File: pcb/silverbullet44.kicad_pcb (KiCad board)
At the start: 2 copper layers, 155.6 x 105.4 mm, 88 parts, among them J1 Conn_01x01, J2 Conn_01x01, J3 Conn_01x01, J4 Conn_01x01, J5 Conn_01x01, SW1 SW_PUSH, SW10 SW_PUSH, SW11 SW_PUSH, SW12 SW_PUSH, SW13 SW_PUSH, SW14 SW_PUSH, SW15 SW_PUSH, SW16 SW_PUSH, SW17 SW_PUSH, SW18 SW_PUSH, SW19 SW_PUSH, SW2 SW_PUSH, SW20 SW_PUSH, SW21 SW_PUSH, SW22 SW_PUSH, SW23 SW_PUSH, SW3 SW_PUSH, SW4 SW_PUSH, SW5 SW_PUSH, SW6 SW_PUSH, SW7 SW_PUSH, SW8 SW_PUSH, SW9 SW_PUSH, U1 ProMicro

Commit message: via
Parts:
- D1, D10, D11, D12, D13, D14, D15, D16, D17, D18, D19, D2, D20, D21, D22, D23, D3, D4, D5, D6, D7, D8, D9: footprint kbd:D3_SMD -> Keyboard:D3_SMD_revese
- J3, J4, J5: footprint keebio_parts:SolidCopper -> MountingHole:MountingHole_2.2mm_M2_Pad_Via
- L1, L10, L11, L12, L13, L14, L15, L16, L17, L18, L19, L2, L20, L21, L22, L3, L4, L5, L6, L7, L8, L9: value SK6812MINI -> YS-SK6812MINI; footprint kbd:SK6812MINI_rev -> Keyboard:YS-SK6812MINI-E-reverse
- SW1, SW10, SW11, SW12, SW13, SW14, SW15, SW16, SW17, SW18, SW2, SW21, SW3, SW4, SW5, SW6, SW7, SW8, SW9: footprint kbd:CherryMX_Hotswap -> Keyboard:MX_Hotswap_R_1u
- SW19, SW20: footprint kbd:CherryMX_Hotswap_1.5u -> Keyboard:MX_Hotswap_R_1.5u
- SW22: footprint kbd:CherryMX_Hotswap -> Keyboard:MX_Hotswap_R_1.25u
- moved L22 127.6 mm to (75.9, 106.6), turned to 300 degrees
- moved L20 96.3 mm to (112.4, 102.9)
- moved L21 92.6 mm to (92.5, 96.9), turned to 300 degrees
- moved L19 89.2 mm to (125.7, 94.6), turned to 90 degrees
- moved L4 61.6 mm to (163.8, 29.2)
- moved L5 58.0 mm to (182.9, 38.1)
- moved L6 57.3 mm to (201.9, 47.6)
- moved L7 53.4 mm to (201.9, 66.7)
- moved L13 45.8 mm to (106.7, 72.4), turned to 0 degrees
- moved L14 44.6 mm to (125.7, 67.3), turned to 0 degrees
- moved L15 43.6 mm to (144.8, 62.9)
- moved L1 39.1 mm to (106.7, 34.3)
- moved L3 39.0 mm to (144.8, 24.8)
- moved L16 38.6 mm to (163.8, 67.3)
- moved L18 33.8 mm to (201.9, 85.7)
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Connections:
- L1 pad 1: Net-(L1-Pad1) -> VCC
- L1 pad 2: GND -> Net-(L1-Pad2)
- L1 pad 3: LED -> GND
- L1 pad 4: VCC -> LED
- L10 pad 1: Net-(L10-Pad1) -> VCC
- L10 pad 2: GND -> Net-(L10-Pad2)
- L10 pad 3: Net-(L10-Pad3) -> GND
- L10 pad 4: VCC -> Net-(L10-Pad4)
- L11 pad 1: Net-(L11-Pad1) -> VCC
- L11 pad 2: GND -> Net-(L11-Pad2)
- L11 pad 3: Net-(L10-Pad1) -> GND
- L11 pad 4: VCC -> Net-(L11-Pad4)
- L12 pad 1: Net-(L12-Pad1) -> VCC
- L12 pad 2: GND -> Net-(L12-Pad2)
- L12 pad 3: Net-(L11-Pad1) -> GND
- L12 pad 4: VCC -> Net-(L10-Pad2)
- L13 pad 1: Net-(L13-Pad1) -> VCC
- L13 pad 2: GND -> Net-(L13-Pad2)
- L13 pad 3: Net-(L12-Pad1) -> GND
- L13 pad 4: VCC -> Net-(L11-Pad2)
- L14 pad 1: Net-(L14-Pad1) -> VCC
- L14 pad 2: GND -> Net-(L14-Pad2)
- L14 pad 3: Net-(L13-Pad1) -> GND
- L14 pad 4: VCC -> Net-(L12-Pad2)
- L15 pad 1: Net-(L15-Pad1) -> VCC
- L15 pad 2: GND -> Net-(L15-Pad2)
- L15 pad 3: Net-(L14-Pad1) -> GND
- L15 pad 4: VCC -> Net-(L13-Pad2)
- L16 pad 1: Net-(L16-Pad1) -> VCC
- L16 pad 2: GND -> Net-(L16-Pad2)
- L16 pad 3: Net-(L15-Pad1) -> GND
- L16 pad 4: VCC -> Net-(L14-Pad2)
- L17 pad 1: Net-(L17-Pad1) -> VCC
- L17 pad 2: GND -> Net-(L17-Pad2)
- L17 pad 3: Net-(L16-Pad1) -> GND
- L17 pad 4: VCC -> Net-(L15-Pad2)
- L18 pad 1: Net-(L18-Pad1) -> VCC
- L18 pad 2: GND -> Net-(L18-Pad2)
- L18 pad 3: Net-(L17-Pad1) -> GND
- L18 pad 4: VCC -> Net-(L16-Pad2)
- L19 pad 1: Net-(L19-Pad1) -> VCC
- L19 pad 2: GND -> Net-(L19-Pad2)
- L19 pad 3: Net-(L18-Pad1) -> GND
- L19 pad 4: VCC -> Net-(L17-Pad2)
- L2 pad 1: Net-(L2-Pad1) -> VCC
- L2 pad 2: GND -> Net-(L2-Pad2)
- L2 pad 3: Net-(L1-Pad1) -> GND
- L2 pad 4: VCC -> Net-(L2-Pad4)
- L20 pad 1: Net-(L20-Pad1) -> VCC
- L20 pad 2: GND -> Net-(L20-Pad2)
- L20 pad 3: Net-(L19-Pad1) -> GND
- L20 pad 4: VCC -> Net-(L18-Pad2)
- L21 pad 1: Net-(L21-Pad1) -> VCC
- L21 pad 2: GND -> Net-(L2-Pad4)
- L21 pad 3: Net-(L20-Pad1) -> GND
- L21 pad 4: VCC -> Net-(L19-Pad2)
- L22 pad 1: Net-(J6-Pad1) -> VCC
- L22 pad 2: GND -> Net-(J6-Pad1)
- L22 pad 3: Net-(L21-Pad1) -> GND
- L22 pad 4: VCC -> Net-(L20-Pad2)
- L3 pad 1: Net-(L3-Pad1) -> VCC
- L3 pad 2: GND -> Net-(L3-Pad2)
- L3 pad 3: Net-(L2-Pad1) -> GND
- L3 pad 4: VCC -> Net-(L1-Pad2)
- L4 pad 1: Net-(L4-Pad1) -> VCC
- L4 pad 2: GND -> Net-(L4-Pad2)
- L4 pad 3: Net-(L3-Pad1) -> GND
- L4 pad 4: VCC -> Net-(L2-Pad2)
- L5 pad 1: Net-(L5-Pad1) -> VCC
- L5 pad 2: GND -> Net-(L5-Pad2)
- L5 pad 3: Net-(L4-Pad1) -> GND
- L5 pad 4: VCC -> Net-(L3-Pad2)
- L6 pad 1: Net-(L6-Pad1) -> VCC
- L6 pad 2: GND -> Net-(L6-Pad2)
- L6 pad 3: Net-(L5-Pad1) -> GND
- L6 pad 4: VCC -> Net-(L4-Pad2)
- L7 pad 1: Net-(L7-Pad1) -> VCC
- L7 pad 2: GND -> Net-(L7-Pad2)
- L7 pad 3: Net-(L6-Pad1) -> GND
- L7 pad 4: VCC -> Net-(L5-Pad2)
- L8 pad 1: Net-(L8-Pad1) -> VCC
- L8 pad 2: GND -> Net-(L10-Pad4)
- L8 pad 3: Net-(L7-Pad1) -> GND
- L8 pad 4: VCC -> Net-(L6-Pad2)
- L9 pad 1: Net-(L10-Pad3) -> VCC
- L9 pad 2: GND -> Net-(L11-Pad4)
- L9 pad 3: Net-(L8-Pad1) -> GND
- L9 pad 4: VCC -> Net-(L7-Pad2)
- Ref1 pad : (no net) -> GND
- Ref2 pad : (no net) -> GND
- Ref3 pad : (no net) -> GND
- Ref5 pad : (no net) -> GND
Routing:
- net GND: track 858.1 -> 96.7 mm, vias 61 -> 22
- net VCC: track 749.9 -> 77.2 mm, vias 23 -> 22
- net COL5: track 271.8 -> 0.00 mm, vias 2 -> 0
- net COL3: track 244.4 -> 0.00 mm, vias 4 -> 0
- net COL2: track 229.4 -> 0.00 mm, vias 4 -> 0
- net COL1: track 227.2 -> 0.00 mm, vias 4 -> 0
- net COL4: track 224.8 -> 0.00 mm, vias 3 -> 0
- net COL0: track 222.9 -> 0.00 mm, vias 4 -> 0
- net ROW2: track 178.4 -> 0.00 mm
- net ROW1: track 163.9 -> 0.00 mm
- net ROW0: track 156.7 -> 0.00 mm, vias 7 -> 6
- net ROW3: track 122.6 -> 0.00 mm
- net Net-(J6-Pad1): track 122.9 -> 7.13 mm
- net LED: track 100.1 -> 7.05 mm
- net BAT+: track 66.1 -> 0.00 mm
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- removed copper zone on B.Cu, net GND
- removed copper zone on F.Cu, net GND

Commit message: promicro
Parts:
- removed J1, J2: Conn_01x01, kbd:1pin_conn
- removed R1, R2: R, keebio_parts:Resistor-Hybrid
- SW23: footprint kbd:ResetSW -> Button_Switch_THT:SW_Tactile_SPST_Angled_PTS645Vx39-2LFS
- moved LS1 34.4 mm to (78.7, 69.2), turned to 0 degrees
- moved R3 33.9 mm to (78.7, 76.2), turned to 180 degrees
- moved J5 19.3 mm to (62.0, 26.0)
- moved D23 18.1 mm to (78.7, 62.9), turned to 0 degrees
- moved TRRS1 6.98 mm to (55.9, 61.0)
- moved SW23 5.24 mm to (59.1, 47.6), turned to 90 degrees
- moved U1 5.06 mm to (80.6, 39.4), turned to 0 degrees
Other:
- outline, holes or cut-outs redrawn

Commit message: power lined
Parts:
- moved TRRS1 25.4 mm to (55.9, 35.6)
- moved LS1 3.42 mm to (75.6, 67.9)
- moved D23 3.42 mm to (75.6, 61.6)
- moved R3 3.42 mm to (75.6, 74.9)
- moved SW23 3.24 mm to (58.4, 50.8)
- renumbered G*** to G*2, G*** to G1
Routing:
- net VCC: track 77.2 -> 550.3 mm
- net GND: track 96.7 -> 463.0 mm
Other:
- outline, holes or cut-outs redrawn

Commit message: deg LED
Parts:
- TRRS1: footprint kbd:MJ-4PP-9 -> Keyboard:MJ-4PP-9
- U1: footprint kbd:ProMicro_v2 -> Keyboard:ProMicro_v2
- moved L7 95.4 mm to (201.9, 66.7), turned to 180 degrees
- moved L20 91.2 mm to (112.4, 102.9), turned to 180 degrees
- moved L17 79.6 mm to (182.9, 76.2)
- moved L14 78.7 mm to (125.7, 67.3)
- moved L18 78.4 mm to (201.9, 85.7)
- moved L6 76.2 mm to (201.9, 47.6)
- moved L13 71.6 mm to (106.7, 72.4)
- moved L11 58.9 mm to (125.7, 48.3), turned to 180 degrees
- moved L10 54.3 mm to (144.8, 43.8), turned to 180 degrees
- moved L4 53.4 mm to (163.8, 29.2)
- moved L19 46.9 mm to (125.7, 94.6), turned to 90 degrees
- moved L3 40.4 mm to (144.8, 24.8)
- moved L15 38.5 mm to (144.8, 62.9)
- moved L8 38.5 mm to (182.9, 57.1), turned to 180 degrees
- moved L9 33.8 mm to (163.8, 48.3), turned to 180 degrees
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- renumbered L19 to L10, L21 to L11, L2 to L12, L4 to L13, L6 to L14, L8 to L15, L10 to L16, L12 to L17, L14 to L18, L16 to L19, L3 to L2, L18 to L20, L20 to L21, L5 to L3, L7 to L4, L9 to L5, L11 to L6, L13 to L7, L15 to L8, L17 to L9
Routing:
- net GND: track 463.0 -> 536.7 mm
- net VCC: track 550.3 -> 587.1 mm
- net Net-(L20-Pad2): track 14.1 -> 13.6 mm
- net Net-(L11-Pad2): track 13.6 -> 14.1 mm

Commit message: route done
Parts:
- added ?: , , F.Cu at (62.2, 43.2)
- moved J5 2.61 mm to (59.7, 24.8)
- moved D1 0.63 mm to (97.2, 36.2)
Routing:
- net GND: track 536.7 -> 937.9 mm, vias 22 -> 72
- net COL3: track 0.00 -> 230.7 mm, vias 0 -> 4
- net COL5: track 0.00 -> 226.9 mm, vias 0 -> 3
- net COL2: track 0.00 -> 217.0 mm, vias 0 -> 4
- net COL1: track 0.00 -> 214.7 mm, vias 0 -> 4
- net COL4: track 0.00 -> 200.0 mm, vias 0 -> 3
- net COL0: track 0.00 -> 197.2 mm, vias 0 -> 4
- net ROW2: track 0.00 -> 195.0 mm, vias 6 -> 7
- net ROW1: track 0.00 -> 178.3 mm, vias 6 -> 8
- net VCC: track 587.1 -> 765.1 mm
- net ROW0: track 0.00 -> 142.4 mm
- net ROW3: track 0.00 -> 120.1 mm
- net Net-(L18-Pad2): track 14.1 -> 132.7 mm
- net BAT+: track 0.00 -> 77.1 mm, vias 0 -> 1
- net Net-(D6-Pad2): track 0.00 -> 62.9 mm
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- added copper zone on B.Cu, net GND
- added copper zone on F.Cu, net GND

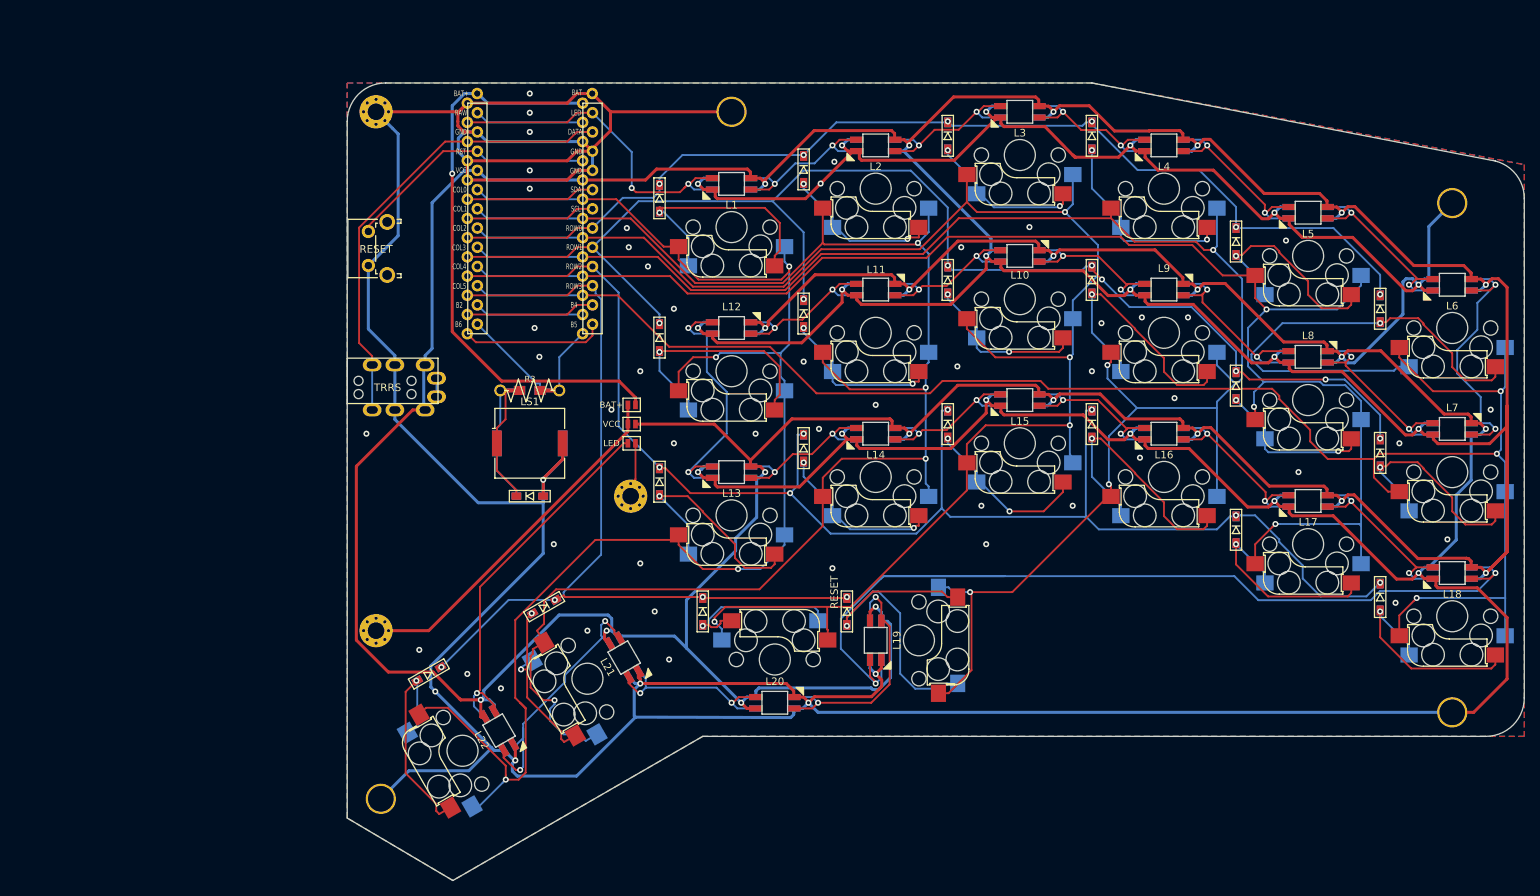
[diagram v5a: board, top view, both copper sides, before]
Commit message: add OLED
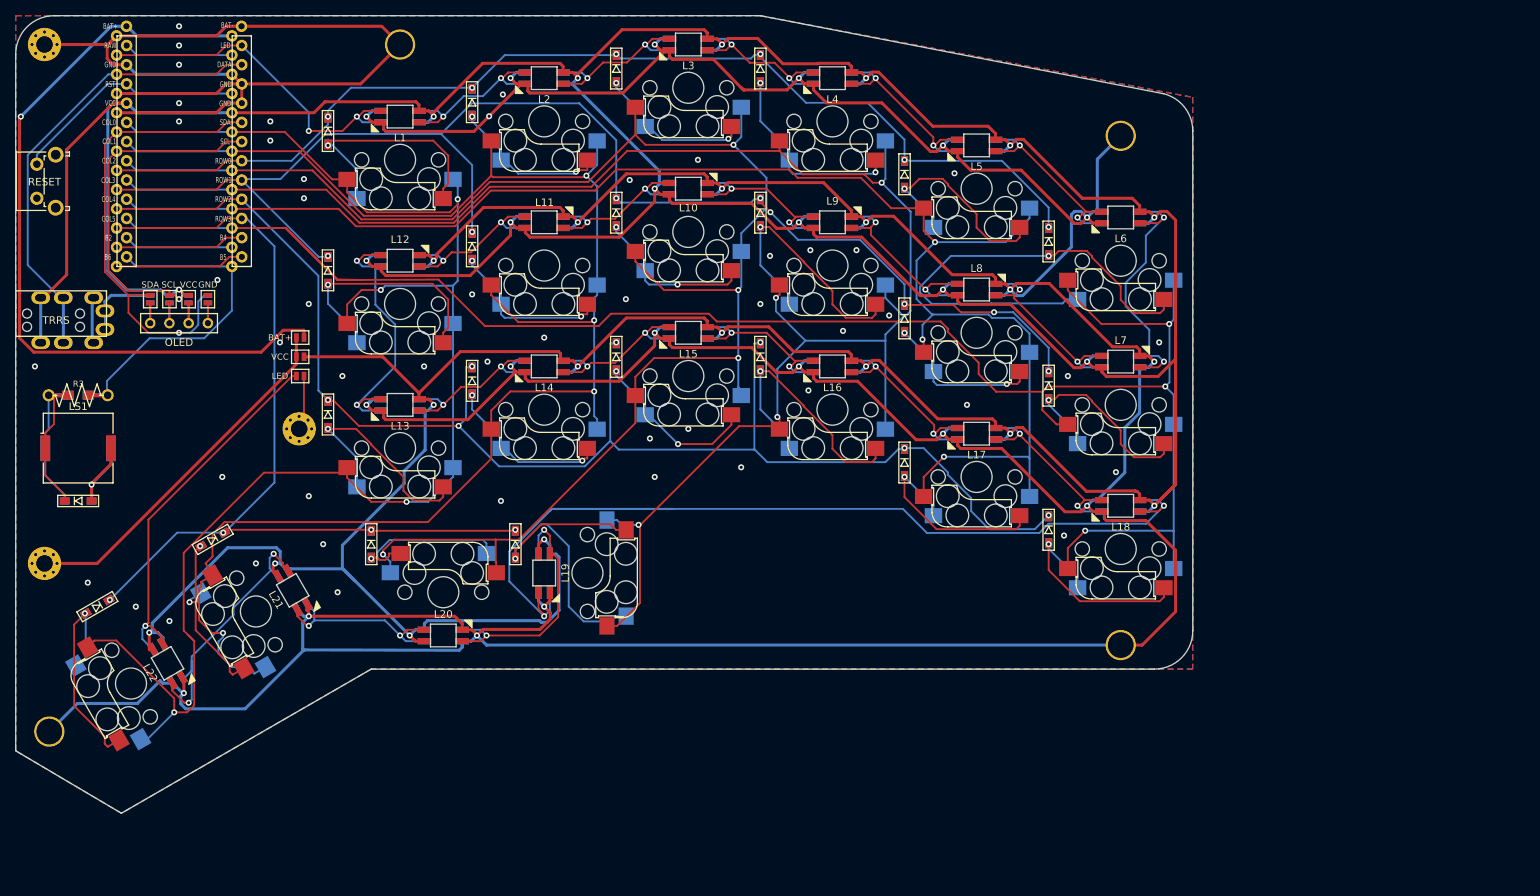
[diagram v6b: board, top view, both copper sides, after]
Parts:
- added J1: Conn_01x04, Keyboard:OLED, F.Cu at (29.8, 52.7)
- added JP10: VCC, kbd:Jumper, B.Cu at (32.4, 49.5)
- added JP11: GND, kbd:Jumper, B.Cu at (29.8, 49.5)
- added JP4: GND, kbd:Jumper, F.Cu at (37.5, 49.5)
- added JP5: VCC, kbd:Jumper, F.Cu at (34.9, 49.5)
- added JP6: SCL, kbd:Jumper, F.Cu at (32.4, 49.5)
- added JP7: SDA, kbd:Jumper, F.Cu at (29.8, 49.5)
- added JP8: SDA, kbd:Jumper, B.Cu at (37.5, 49.5)
- added JP9: SCL, kbd:Jumper, B.Cu at (34.9, 49.5)
- moved D23 59.7 mm to (20.3, 76.2)
- moved LS1 59.7 mm to (20.3, 69.2)
- moved R3 59.7 mm to (20.3, 62.2)
- moved U1 47.2 mm to (34.3, 30.5)
- moved G*2 44.9 mm to (118.6, 87.4)
- moved D10 44.7 mm to (110.5, 38.1)
- moved D16 44.7 mm to (110.5, 57.1)
- moved D4 44.7 mm to (110.5, 19.1)
- moved L16 44.7 mm to (120.0, 58.4)
- moved L4 44.7 mm to (120.0, 20.3)
- moved L9 44.7 mm to (120.0, 39.4)
- moved SW10 44.7 mm to (120.0, 45.1)
- moved SW16 44.7 mm to (120.0, 64.1)
- moved SW4 44.7 mm to (120.0, 26.0)
- moved D20 44.7 mm to (38.1, 81.3)
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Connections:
- TRRS1 pad A: Net-(J1-Pad1) -> GND
- TRRS1 pad B: DATA -> VCC
- TRRS1 pad C: GND -> DATA
- TRRS1 pad D: VCC -> GND
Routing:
- net GND: track 937.9 -> 849.6 mm
- net SDA: track 17.1 -> 61.2 mm, vias 0 -> 1
- net SCL: track 17.1 -> 46.0 mm, vias 0 -> 1
- net BAT+: track 77.1 -> 103.2 mm
- net COL5: track 226.9 -> 246.8 mm
- net SPEKER: track 26.3 -> 45.2 mm
- net VCC: track 765.1 -> 752.7 mm, vias 22 -> 23
- net Net-(J1-Pad4): track 0.00 -> 5.35 mm
- net Net-(J1-Pad3): track 0.00 -> 5.35 mm
- net Net-(J1-Pad2): track 0.00 -> 5.35 mm
- net ROW1: track 178.3 -> 182.8 mm
- net Net-(J1-Pad1): track 2.45 -> 5.35 mm
- net COL3: track 230.7 -> 233.3 mm
- net COL0: track 197.2 -> 199.8 mm
- net COL2: track 217.0 -> 219.6 mm
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
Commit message: Its time to requiem
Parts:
- moved J3 38.1 mm to (15.9, 84.5)
- moved J4 38.1 mm to (49.5, 66.7)
- turned JP1 to 180 degrees
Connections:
- TRRS1 pad A: GND -> VCC
- TRRS1 pad B: VCC -> GND
- TRRS1 pad C: DATA -> Net-(TRRS1-PadC)
- TRRS1 pad D: GND -> DATA
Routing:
- net GND: track 849.6 -> 888.5 mm
- net Net-(J3-Pad1): track 16.3 -> 54.9 mm
- net Net-(J4-Pad1): track 56.9 -> 23.4 mm, vias 0 -> 1
- net VCC: track 752.7 -> 723.0 mm
- net Net-(TRRS1-PadC): track 0.00 -> 6.35 mm
- net DATA: track 60.2 -> 61.8 mm

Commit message: fix TRRS and silk, and Add honeycomb acril shield
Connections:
- TRRS1 pad A: VCC -> GND
- TRRS1 pad B: GND -> VCC
- TRRS1 pad C: Net-(TRRS1-PadC) -> DATA
- TRRS1 pad D: DATA -> Net-(TRRS1-PadD)
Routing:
- net VCC: track 723.0 -> 756.3 mm
- net GND: track 888.5 -> 859.2 mm, vias 72 -> 68
- net Net-(TRRS1-PadC): track 6.35 -> 0.00 mm
- net Net-(TRRS1-PadD): track 0.00 -> 6.11 mm
- net DATA: track 61.8 -> 60.5 mm
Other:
- board text added: "Jump Left Hand"
- board text added: "Jump Right Hand"
- board text added: "L1"
- board text added: "L10"
- board text added: "L11"
- board text added: "L12"
- board text added: "L13"
- board text added: "L14"
- board text added: "L15"
- board text added: "L16"
- board text added: "L17"
- board text added: "L18"
- board text added: "L19"
- board text added: "L2"
- board text added: "L20"
- board text added: "L21"
- board text added: "L22"
- board text added: "L3"
- board text added: "L4"
- board text added: "L5"
- board text added: "L6"
- board text added: "L7"
- board text added: "L8"
- board text added: "L9"
